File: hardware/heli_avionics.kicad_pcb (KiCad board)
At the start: 4 copper layers, 65.5 x 39 mm, 73 parts, among them J1 Pin_Header_2x3, J10 Pin_Header_1x1, J2 JST_PH_01x02, J3 JST_XH_01x02, J4 JST_XH_01x02, J5 JST_PH_01x03, J6 Conn_01x01, J7 JST_ZH_01x02, J8 Conn_01x01, J9 Pin_Header_1x2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

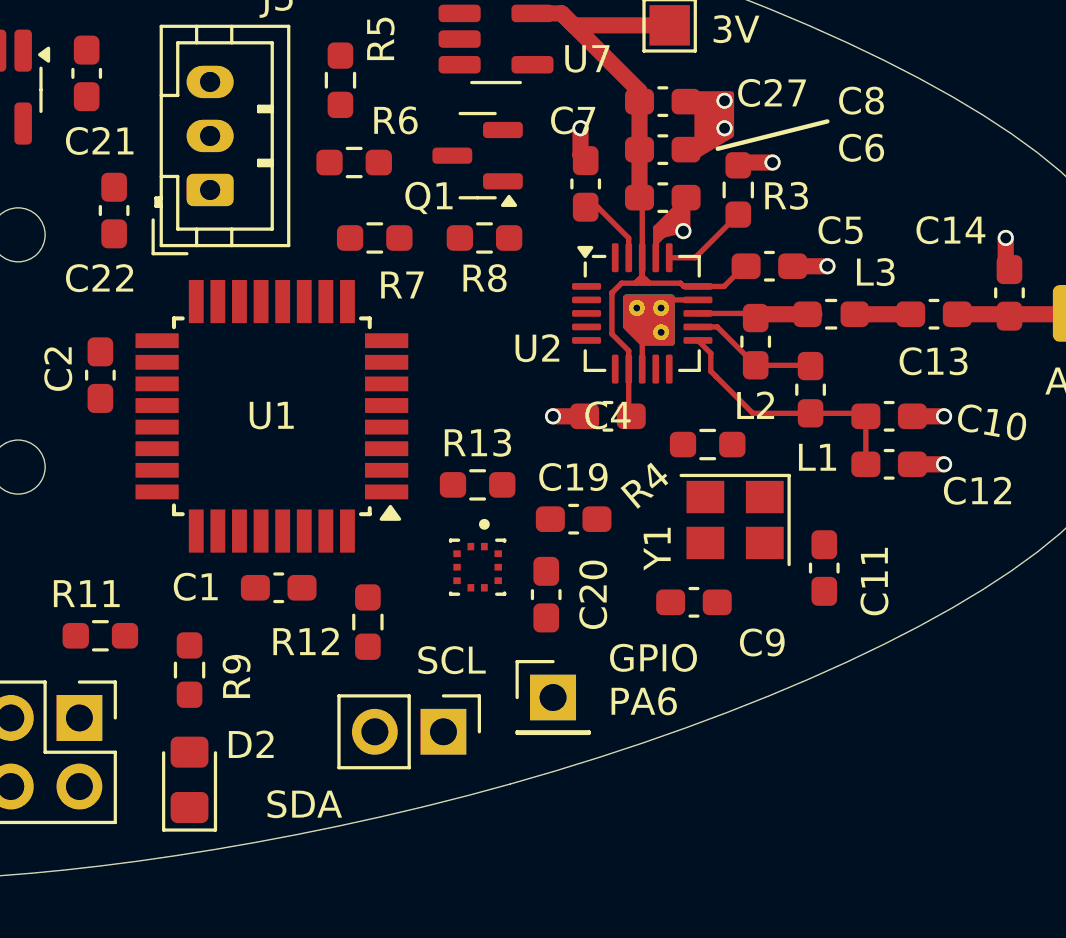
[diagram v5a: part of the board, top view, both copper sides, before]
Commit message: Routed most pressure sensor traces
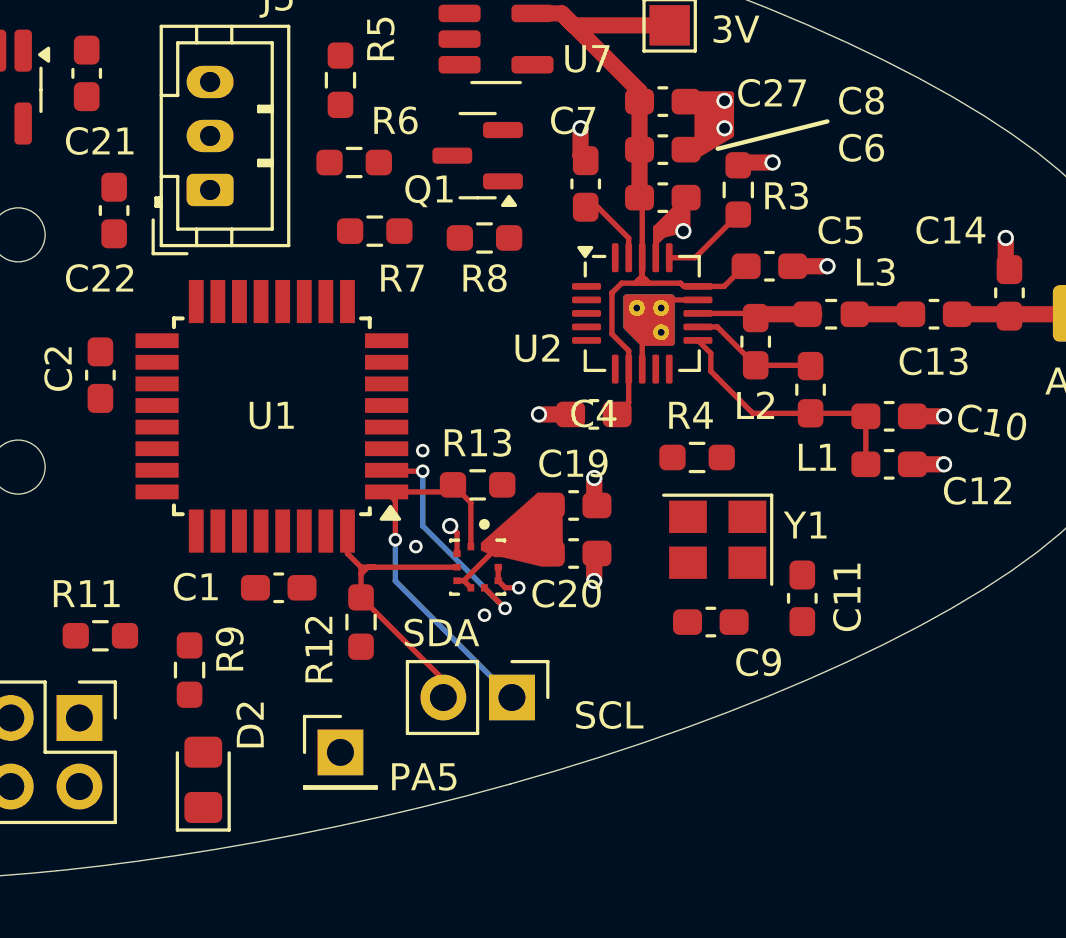
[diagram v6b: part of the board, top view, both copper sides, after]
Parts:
- moved J10 8.13 mm to (135.6, 134.4)
- moved J9 2.84 mm to (142.0, 132.3)
- moved C20 1.83 mm to (144.3, 127.0), turned to 0 degrees
- moved C11 1.39 mm to (152.7, 128.7)
- moved Y1 0.98 mm to (149.6, 126.5)
- moved C9 0.96 mm to (149.4, 129.5)
- moved R4 0.62 mm to (148.8, 123.4)
- moved C4 0.53 mm to (145.0, 121.8)
- moved C19 0.51 mm to (144.3, 125.2)
- moved D2 0.51 mm to (130.6, 135.4)
- moved R7 0.25 mm to (136.9, 115.1)
- moved R12 0.25 mm to (136.4, 129.5)
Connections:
- U1 pad 13: /PD3 -> unconnected-(U1-PD3-Pad13)
- U1 pad 14: /PD4 -> unconnected-(U1-PD4-Pad14)
- U1 pad 15: /PD5 -> unconnected-(U1-PD5-Pad15)
- U2 pad 21: GND -> (no net)
- U5 pad 5: GND -> VCC
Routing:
- net /I2C_SCL: track 0.00 -> 14.7 mm, vias 0 -> 1
- net /I2C_SDA: track 0.00 -> 11.9 mm
- net /PA4: track 0.00 -> 8.78 mm, vias 0 -> 2
- net GND: track 17.9 -> 22.7 mm, vias 10 -> 17
- net VCC: track 0.00 -> 3.60 mm
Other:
- board text added: "PA5"
- board text removed: "GPIO PA6"

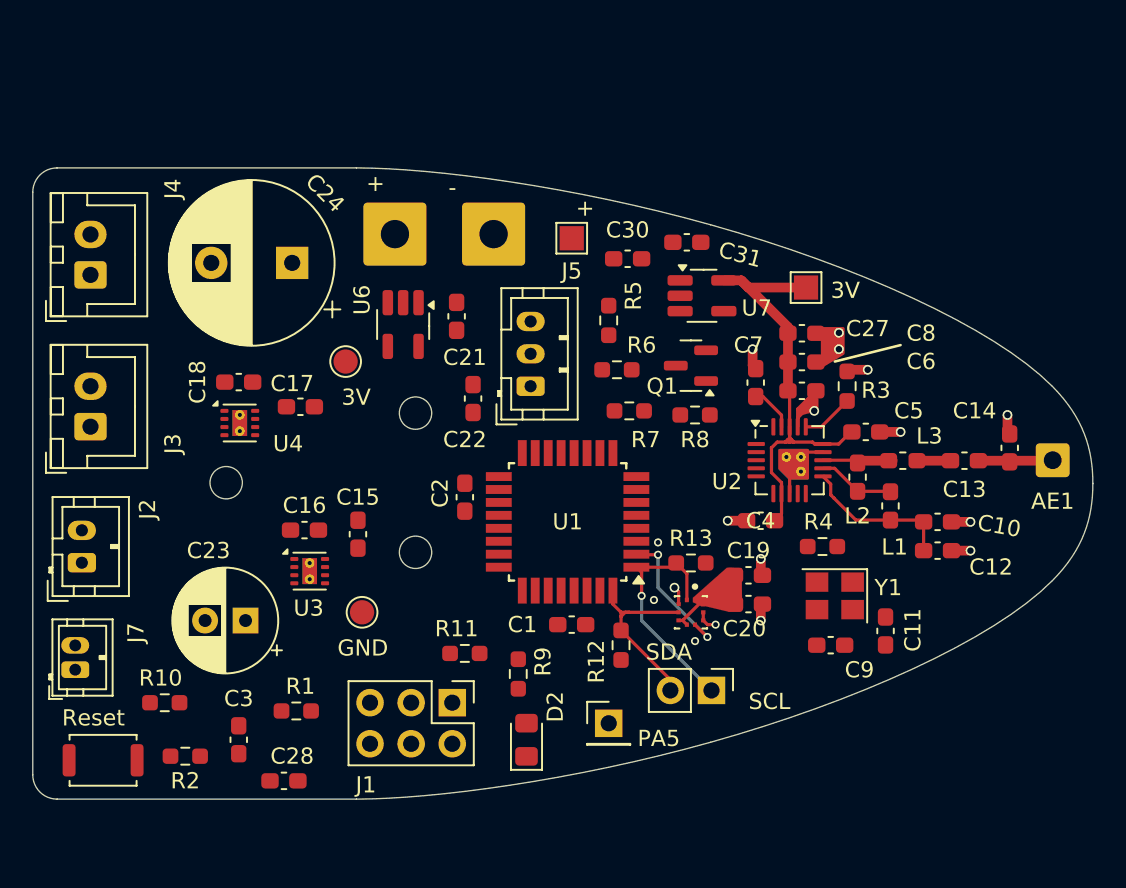
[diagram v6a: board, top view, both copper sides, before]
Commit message: Routed decoupling caps and PWM traces
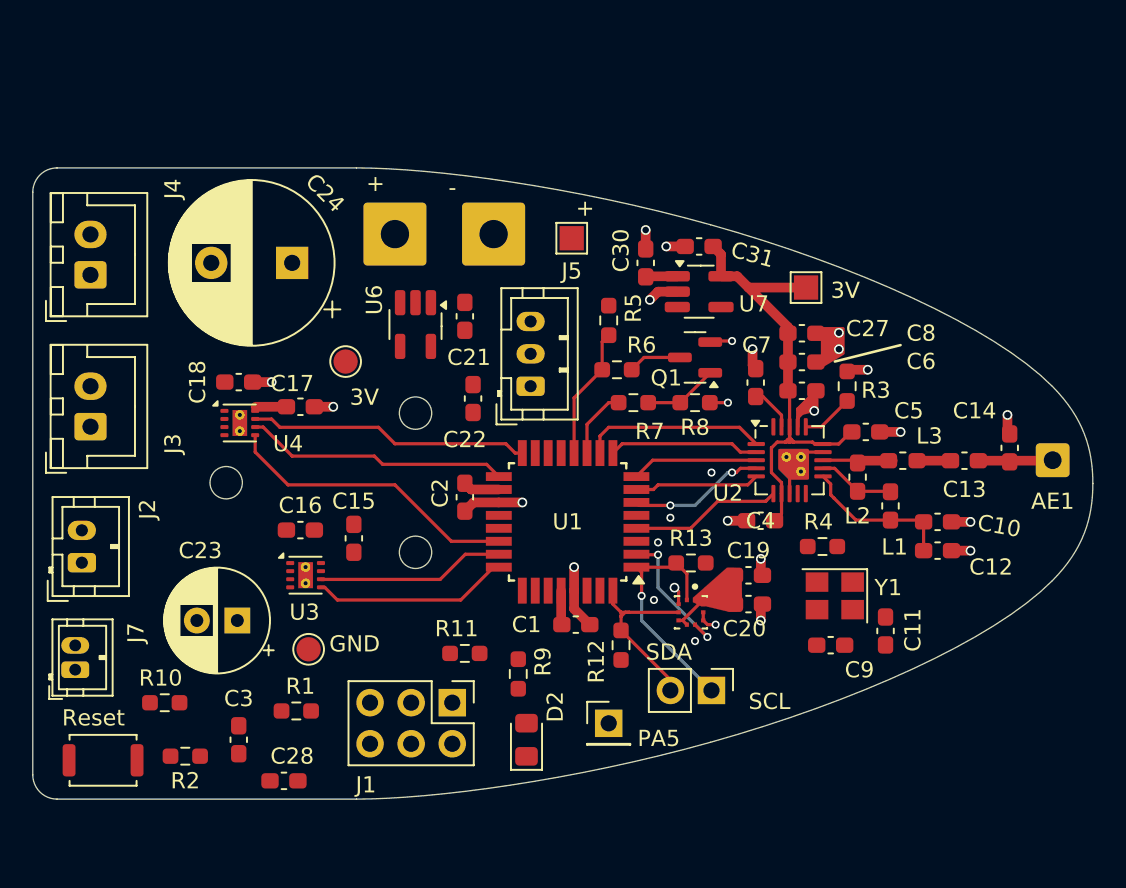
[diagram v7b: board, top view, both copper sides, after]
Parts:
- moved TP4 4.02 mm to (117.1, 129.8)
- moved C30 1.15 mm to (137.9, 105.9), turned to 90 degrees
- moved C31 0.80 mm to (141.2, 104.9)
- moved R8 0.76 mm to (141.0, 114.6)
- moved U6 0.76 mm to (123.7, 109.7)
- moved Q1 0.57 mm to (141.0, 111.8)
- moved R7 0.57 mm to (137.2, 114.6)
- moved C23 0.51 mm to (112.7, 128.0)
- moved C21 0.51 mm to (126.7, 109.2)
- moved C15 0.36 mm to (119.9, 122.9)
- moved U3 0.36 mm to (116.9, 125.2)
- moved U7 0.31 mm to (141.2, 107.7)
- moved C1 0.25 mm to (133.6, 128.3)
- moved C16 0.25 mm to (116.6, 122.4)
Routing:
- net /PF2: track 0.00 -> 18.4 mm
- net /PD6: track 0.00 -> 17.4 mm
- net GND: track 22.7 -> 39.5 mm, vias 17 -> 28
- net /PD7: track 0.00 -> 16.3 mm
- net /PF4: track 0.00 -> 12.2 mm
- net /PF3: track 0.00 -> 11.6 mm
- net /PD0: track 0.00 -> 11.4 mm
- net /PA6: track 0.00 -> 9.36 mm
- net /SPI_SS: track 0.00 -> 9.31 mm
- net /SPI_MOSI: track 0.00 -> 8.43 mm, vias 0 -> 2
- net /PD2: track 0.00 -> 8.17 mm
- net /SPI_CLK: track 0.00 -> 7.82 mm
- net /SPI_MISO: track 0.00 -> 7.74 mm
- net VCC: track 3.60 -> 10.2 mm
- net Net-(Q1-G): track 0.00 -> 4.60 mm
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
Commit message: Fixed motor driver grounding
Made new footprint with smaller thermal vias for less solder wicking.
Added more vias in ground puddle.
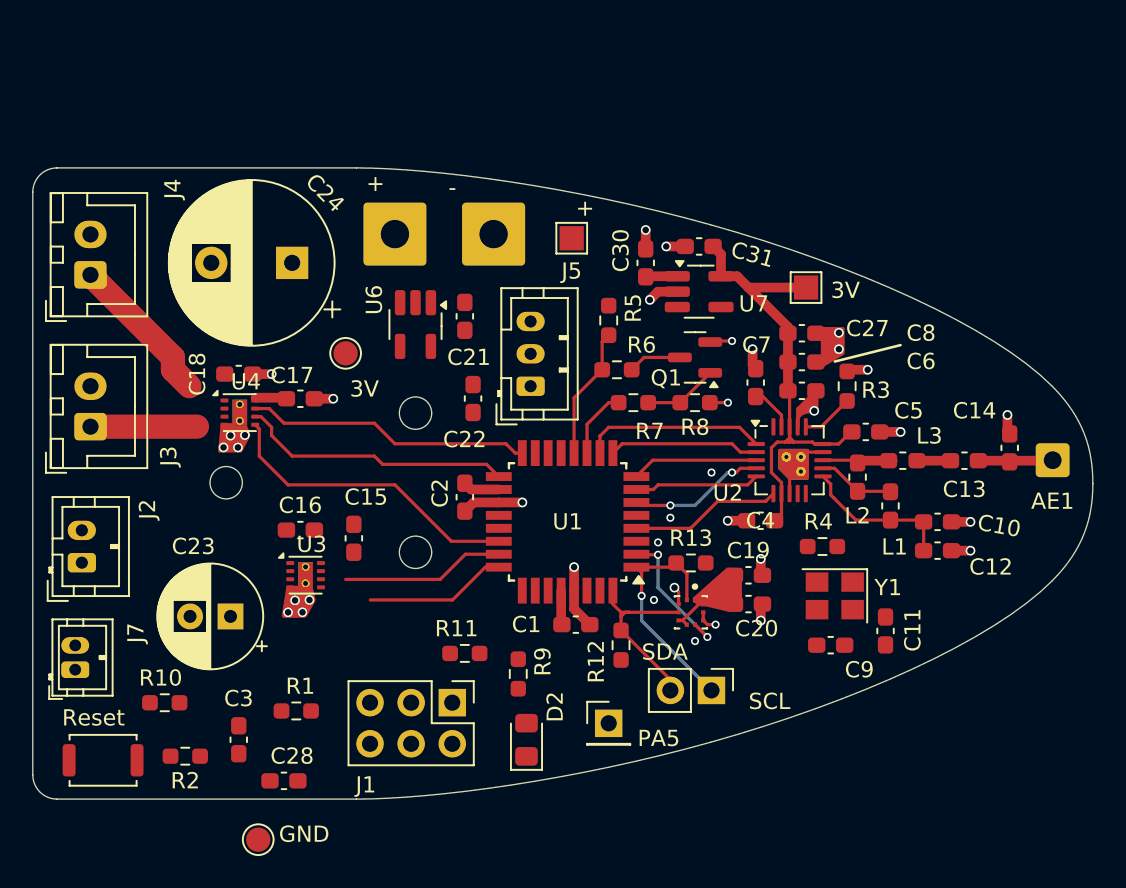
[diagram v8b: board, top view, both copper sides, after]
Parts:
- U3, U4: footprint Package_SON:WSON-8-1EP_2x2mm_P0.5mm_EP0.9x1.6mm_ThermalVias -> heli-footprints:WSON-8-1EP_2x2mm_P0.5mm_EP0.9x1.6mm_ThermalVias
- moved TP4 12.2 mm to (114.0, 141.6)
- moved U4 0.64 mm to (112.8, 115.2)
- moved TP2 0.51 mm to (119.4, 111.5)
- moved C17 0.50 mm to (116.6, 114.3)
- moved C18 0.50 mm to (112.8, 112.8)
- moved C23 0.49 mm to (112.3, 127.8)
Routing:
- net Net-(J4-Pin_1): track 0.00 -> 9.41 mm
- net Net-(J3-Pin_1): track 0.00 -> 6.58 mm
- net /PF4: track 12.2 -> 8.78 mm
- net /PF3: track 11.6 -> 10.1 mm
- net GND: track 39.5 -> 40.9 mm, vias 28 -> 36
- net /PF2: track 18.4 -> 19.0 mm
- net /PD7: track 16.3 -> 16.9 mm
